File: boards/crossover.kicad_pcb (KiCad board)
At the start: 2 copper layers, 44 parts, among them CON1 12VDC Power, J1 JACK_TRS_6PINS, U1 TL074, U2 TL074

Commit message: upadated boards
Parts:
- removed CON1: 12VDC Power, Connect:BARREL_JACK
- added C23: 100n, Capacitors_ThroughHole:C_Disc_D6_P5, F.Cu at (227.3, 127.3)
- added C24: 100n, Capacitors_ThroughHole:C_Disc_D6_P5, F.Cu at (241.6, 108.7)
- added C25: 100n, Capacitors_ThroughHole:C_Disc_D6_P5, F.Cu at (250.2, 97.7)
- added C26: 100n, Capacitors_ThroughHole:C_Disc_D6_P5, F.Cu at (281.5, 69.3)
- added C27: 100n, Capacitors_ThroughHole:C_Disc_D6_P5, F.Cu at (233.1, 118.2)
- added C28: 100n, Capacitors_ThroughHole:C_Disc_D6_P5, F.Cu at (257.8, 97.4)
- added D1: Diode_Bridge, Diodes_ThroughHole:Diode_Bridge_15.7x15.7, F.Cu at (219.2, 69.4)
- added P1: 12-0-12, Terminal_Blocks:TerminalBlock_Pheonix_MKDS1.5-3pol, F.Cu at (187.8, 109.8)
- added R19: 2RH, Resistors_ThroughHole:Resistor_Horizontal_RM10mm, F.Cu at (231.7, 89.8)
- added U3: TDA7292, TO_SOT_Packages_THT:Multiwatt_15_Vertical, F.Cu at (169.5, 76.5)
- C1, C2: value 220u -> 100n; footprint Capacitors_ThroughHole:C_Radial_D10_L13_P5 -> Capacitors_ThroughHole:C_Disc_D3_P2.5
- C10, C17, C18: value 200n -> 100n; footprint Capacitors_SMD:C_0603_HandSoldering -> Capacitors_ThroughHole:C_Disc_D6_P5
- C11, C12, C19, C20, C21, C22, C5, C6, C7, C8, C9: footprint Capacitors_SMD:C_0603_HandSoldering -> Capacitors_ThroughHole:C_Disc_D6_P5
- C13, C14, C15, C16: footprint Capacitors_SMD:C_0603_HandSoldering -> Capacitors_ThroughHole:C_Disc_D3_P2.5
- C3: value 100n -> 6800u; footprint Capacitors_SMD:C_0603_HandSoldering -> Capacitors_ThroughHole:C_Radial_D16_L31.5_P7.5
- C4: value 200n -> 6800u; footprint Capacitors_SMD:C_0603_HandSoldering -> Capacitors_ThroughHole:C_Radial_D16_L31.5_P7.5
- R1: value 4K7 -> 100; footprint Resistors_ThroughHole:Resistor_Horizontal_RM15mm -> Resistors_ThroughHole:Resistor_Horizontal_RM10mm
- R10, R12, R14, R16, R18, R5, R9: footprint Resistors_ThroughHole:Resistor_Horizontal_RM15mm -> Resistors_ThroughHole:Resistor_Horizontal_RM10mm
- R11: value RL -> 2RH; footprint Resistors_ThroughHole:Resistor_Horizontal_RM15mm -> Resistors_ThroughHole:Resistor_Horizontal_RM10mm
- R13, R4, R8: value RH -> RL; footprint Resistors_ThroughHole:Resistor_Horizontal_RM15mm -> Resistors_ThroughHole:Resistor_Horizontal_RM10mm
- R15, R7: value RL -> RH; footprint Resistors_ThroughHole:Resistor_Horizontal_RM15mm -> Resistors_ThroughHole:Resistor_Horizontal_RM10mm
- R17: value 2RH -> RL; footprint Resistors_ThroughHole:Resistor_Horizontal_RM15mm -> Resistors_ThroughHole:Resistor_Horizontal_RM10mm
- R2: value 4K7 -> something bigg-ish; footprint Resistors_ThroughHole:Resistor_Horizontal_RM15mm -> Resistors_ThroughHole:Resistor_Horizontal_RM10mm
- R3: value RL -> something bigg-sh; footprint Resistors_ThroughHole:Resistor_Horizontal_RM15mm -> Resistors_ThroughHole:Resistor_Horizontal_RM10mm
- R6: value 2RH -> RH; footprint Resistors_ThroughHole:Resistor_Horizontal_RM15mm -> Resistors_ThroughHole:Resistor_Horizontal_RM10mm
- moved C8 139.7 mm to (265.3, 87.9)
- moved C7 120.3 mm to (241.6, 117.9)
- moved C6 115.7 mm to (257.7, 106.5)
- moved R4 112.1 mm to (234.7, 69.3)
- moved R5 92.3 mm to (218.5, 89.8)
- moved C2 83.1 mm to (180.2, 88.6)
- moved C5 79.9 mm to (250.2, 106.8)
- moved J1 78.3 mm to (201.2, 70.5)
- moved R9 73.8 mm to (247.9, 69.3)
- moved C16 64.5 mm to (234.7, 126.3)
- moved R10 62.6 mm to (199.5, 121.3)
- moved R2 59.2 mm to (170.3, 127.4)
- moved R11 56.0 mm to (228.7, 108.7)
- moved C1 55.9 mm to (180.2, 95.7)
- moved R3 55.9 mm to (204.4, 89.8)
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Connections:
- C1 pad 1: +6V -> +12V
- C11 pad 2: Net-(C11-Pad2) -> GND
- C13 pad 2: +6V -> +12V
- C14 pad 1: -6V -> -12V
- C15 pad 1: Net-(C15-Pad1) -> GND
- C15 pad 2: Net-(C15-Pad2) -> +12V
- C16 pad 1: Net-(C16-Pad1) -> -12V
- C16 pad 2: Net-(C16-Pad2) -> GND
- C18 pad 1: left_low_out -> Net-(C18-Pad1)
- C19 pad 1: Net-(C19-Pad1) -> right_low_out
- C19 pad 2: Net-(C15-Pad1) -> Net-(C19-Pad2)
- C2 pad 2: -6V -> -12V
- C20 pad 1: Net-(C20-Pad1) -> left_low_out
- C20 pad 2: Net-(C16-Pad1) -> Net-(C20-Pad2)
- C21 pad 2: GND -> Net-(C17-Pad1)
- C22 pad 2: GND -> Net-(C18-Pad1)
- C3 pad 1: Net-(C3-Pad1) -> +12V
- C3 pad 2: right_in -> GND
- C4 pad 1: Net-(C4-Pad1) -> GND
- C4 pad 2: Net-(C4-Pad2) -> -12V
- C5 pad 2: Net-(C3-Pad1) -> right_in
- C6 pad 1: Net-(C6-Pad1) -> Net-(C10-Pad2)
- C6 pad 2: GND -> left_in
- C7 pad 1: GND -> Net-(C25-Pad1)
- C7 pad 2: +6V -> Net-(C25-Pad2)
- C8 pad 1: -6V -> Net-(C8-Pad1)
- C8 pad 2: GND -> Net-(C8-Pad2)
- C9 pad 1: Net-(C11-Pad2) -> Net-(C9-Pad1)
- C9 pad 2: left_in -> Net-(C5-Pad1)
- J1 pad 4: Net-(J1-Pad4) -> (no net)
- J1 pad 5: Net-(J1-Pad5) -> (no net)
- J1 pad 6: Net-(J1-Pad6) -> (no net)
- R1 pad 1: +6V -> GND
- R1 pad 2: GND -> (no net)
- R10 pad 2: Net-(C11-Pad1) -> Net-(C9-Pad1)
- R11 pad 1: Net-(C4-Pad1) -> GND
- R11 pad 2: Net-(C17-Pad2) -> Net-(C10-Pad1)
- R12 pad 1: Net-(C10-Pad1) -> Net-(C25-Pad1)
- R12 pad 2: Net-(C18-Pad2) -> Net-(C19-Pad2)
- R13 pad 1: Net-(C15-Pad1) -> Net-(C8-Pad1)
- R13 pad 2: right_high_out -> Net-(C20-Pad2)
- R14 pad 1: Net-(C16-Pad1) -> Net-(C17-Pad1)
- R14 pad 2: left_high_out -> right_high_out
- R15 pad 1: Net-(C21-Pad1) -> Net-(C18-Pad1)
- R15 pad 2: Net-(C17-Pad2) -> left_high_out
- R16 pad 1: Net-(C22-Pad1) -> Net-(C23-Pad1)
- R16 pad 2: Net-(C18-Pad2) -> Net-(C19-Pad2)
- R17 pad 1: GND -> Net-(C24-Pad1)
- R17 pad 2: Net-(C19-Pad1) -> Net-(C20-Pad2)
- R18 pad 2: Net-(C20-Pad1) -> Net-(C21-Pad1)
- R2 pad 1: GND -> +12V
- R2 pad 2: -6V -> GND
- R3 pad 1: right_in -> GND
- R3 pad 2: Net-(C4-Pad2) -> -12V
- R4 pad 1: Net-(C3-Pad1) -> right_in
- R4 pad 2: Net-(C15-Pad2) -> Net-(C25-Pad2)
- R5 pad 1: Net-(C6-Pad1) -> left_in
- R5 pad 2: Net-(C4-Pad2) -> Net-(C8-Pad2)
- R6 pad 1: GND -> Net-(C5-Pad1)
- R6 pad 2: Net-(C5-Pad1) -> Net-(C17-Pad2)
- R7 pad 1: left_in -> Net-(C10-Pad2)
- R7 pad 2: Net-(C10-Pad2) -> Net-(C18-Pad2)
- R8 pad 1: Net-(C11-Pad2) -> Net-(C11-Pad1)
- R8 pad 2: Net-(C16-Pad2) -> Net-(C25-Pad2)
- R9 pad 2: Net-(C10-Pad2) -> Net-(C8-Pad2)
- U1 pad 1: Net-(C4-Pad1) -> Net-(C25-Pad1)
- U1 pad 10: Net-(C21-Pad1) -> Net-(C12-Pad1)
- U1 pad 11: -6V -> -12V
- U1 pad 12: Net-(C19-Pad1) -> Net-(C10-Pad1)
- U1 pad 13: right_high_out -> Net-(C18-Pad2)
- U1 pad 14: right_high_out -> Net-(C18-Pad2)
- U1 pad 2: Net-(C4-Pad1) -> Net-(C25-Pad1)
- U1 pad 3: Net-(C6-Pad1) -> Net-(C11-Pad1)
- U1 pad 4: +6V -> +12V
- U1 pad 5: Net-(C5-Pad1) -> Net-(C9-Pad1)
- U1 pad 6: Net-(C15-Pad2) -> Net-(C17-Pad2)
- U1 pad 7: Net-(C15-Pad2) -> Net-(C17-Pad2)
- U1 pad 8: Net-(C17-Pad1) -> Net-(C8-Pad1)
- U1 pad 9: Net-(C17-Pad1) -> Net-(C8-Pad1)
- U2 pad 1: Net-(C10-Pad1) -> right_high_out
- U2 pad 10: Net-(C20-Pad1) -> Net-(C23-Pad1)
- U2 pad 11: -6V -> (no net)
- U2 pad 12: Net-(C22-Pad1) -> Net-(C24-Pad1)
- U2 pad 2: Net-(C10-Pad1) -> right_high_out
- U2 pad 3: Net-(C12-Pad1) -> Net-(C21-Pad1)
- U2 pad 4: +6V -> (no net)
- U2 pad 5: Net-(C11-Pad1) -> Net-(C22-Pad1)
- U2 pad 6: Net-(C16-Pad2) -> left_high_out
- U2 pad 7: Net-(C16-Pad2) -> left_high_out
- U2 pad 8: left_high_out -> right_low_out
- U2 pad 9: left_high_out -> right_low_out
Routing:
- net Net-(C10-Pad2): track 155.9 -> 0.00 mm, vias 2 -> 0
- net Net-(C12-Pad1): track 153.7 -> 0.00 mm, vias 1 -> 0
- net Net-(C21-Pad1): track 142.9 -> 0.00 mm, vias 1 -> 0
- net GND: track 141.8 -> 0.00 mm
- net Net-(C10-Pad1): track 121.5 -> 0.00 mm
- net +6V: track 113.5 -> 0.00 mm, vias 1 -> 0
- net Net-(C11-Pad1): track 90.0 -> 0.00 mm, vias 1 -> 0
- net right_high_out: track 84.7 -> 0.00 mm, vias 1 -> 0
- net Net-(C17-Pad2): track 75.8 -> 0.00 mm, vias 1 -> 0
- net -6V: track 72.8 -> 0.00 mm
- net Net-(C22-Pad1): track 70.5 -> 0.00 mm
- net Net-(C20-Pad1): track 69.1 -> 0.00 mm, vias 1 -> 0
- net left_in: track 64.3 -> 0.00 mm, vias 1 -> 0
- net Net-(C4-Pad2): track 42.8 -> 0.00 mm
- net left_high_out: track 42.5 -> 0.00 mm
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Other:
- net class Default: via_dia 0.381 -> 0.6858; via_drill 0.254 -> 0.3302
- net class Power: via_dia 0.381 -> 0.6858; via_drill 0.254 -> 0.3302
- rule via_min_drill: 0.254 -> 0.3302
- rule via_min_size: 0.381 -> 0.6858

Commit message: some board work, added windows appveyor file
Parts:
- added REF***: OSHW-Logo_5.7x6mm_SilkScreen, Symbols:OSHW-Logo_5.7x6mm_SilkScreen, F.Cu at (132.1, 61.0)
- added REF***: KiCad-Logo2_6mm_SilkScreen, Symbols:KiCad-Logo2_6mm_SilkScreen, F.Cu at (119.4, 61.0)
- added U5: LM7815CT, TO-220, F.Cu at (215.9, 66.0)
- added U6: LM7915CT, TO-220, F.Cu at (212.1, 74.9)
- R2: value something bigg-ish -> 1K 1W
- R3: value something bigg-sh -> 1K 1W
- moved C26 135.1 mm to (147.3, 85.0), turned to 90 degrees
- moved C8 107.0 mm to (158.8, 97.8)
- moved C13 104.6 mm to (198.1, 138.4)
- moved C14 95.4 mm to (172.7, 119.4)
- moved R9 95.0 mm to (154.9, 88.9)
- moved C16 75.0 mm to (160.0, 119.4)
- moved C12 71.7 mm to (172.7, 83.8)
- moved R10 68.8 mm to (132.1, 108.0)
- moved C11 67.9 mm to (207.0, 108.0)
- moved J1 66.4 mm to (236.2, 127.0)
- moved R4 66.4 mm to (217.2, 133.3)
- moved C15 65.8 mm to (198.1, 144.8)
- moved C6 62.9 mm to (212.1, 149.9)
- moved D1 62.5 mm to (181.6, 119.4)
- moved U2 61.6 mm to (231.1, 92.7)
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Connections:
- C26 pad 1: (no net) -> Net-(C26-Pad1)
- C26 pad 2: (no net) -> Net-(C26-Pad2)
- C27 pad 1: (no net) -> right_low_out
- C27 pad 2: (no net) -> Net-(C19-Pad2)
- C28 pad 1: (no net) -> left_low_out
- C28 pad 2: (no net) -> Net-(C20-Pad2)
- C8 pad 1: Net-(C8-Pad1) -> Net-(C26-Pad1)
- C8 pad 2: Net-(C8-Pad2) -> Net-(C26-Pad2)
- J1 pad 2: right_in -> left_in
- J1 pad 3: left_in -> right_in
- R13 pad 1: Net-(C8-Pad1) -> Net-(C26-Pad1)
- R5 pad 2: Net-(C8-Pad2) -> Net-(C26-Pad2)
- R9 pad 2: Net-(C8-Pad2) -> Net-(C26-Pad2)
- U1 pad 8: Net-(C8-Pad1) -> Net-(C26-Pad1)
- U1 pad 9: Net-(C8-Pad1) -> Net-(C26-Pad1)
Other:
- board outline added: 160 x 105.4 mm
- net class Audio Out added: clearance 0.254, trace_width 1.27, via_dia 0.6858, via_drill 0.3302

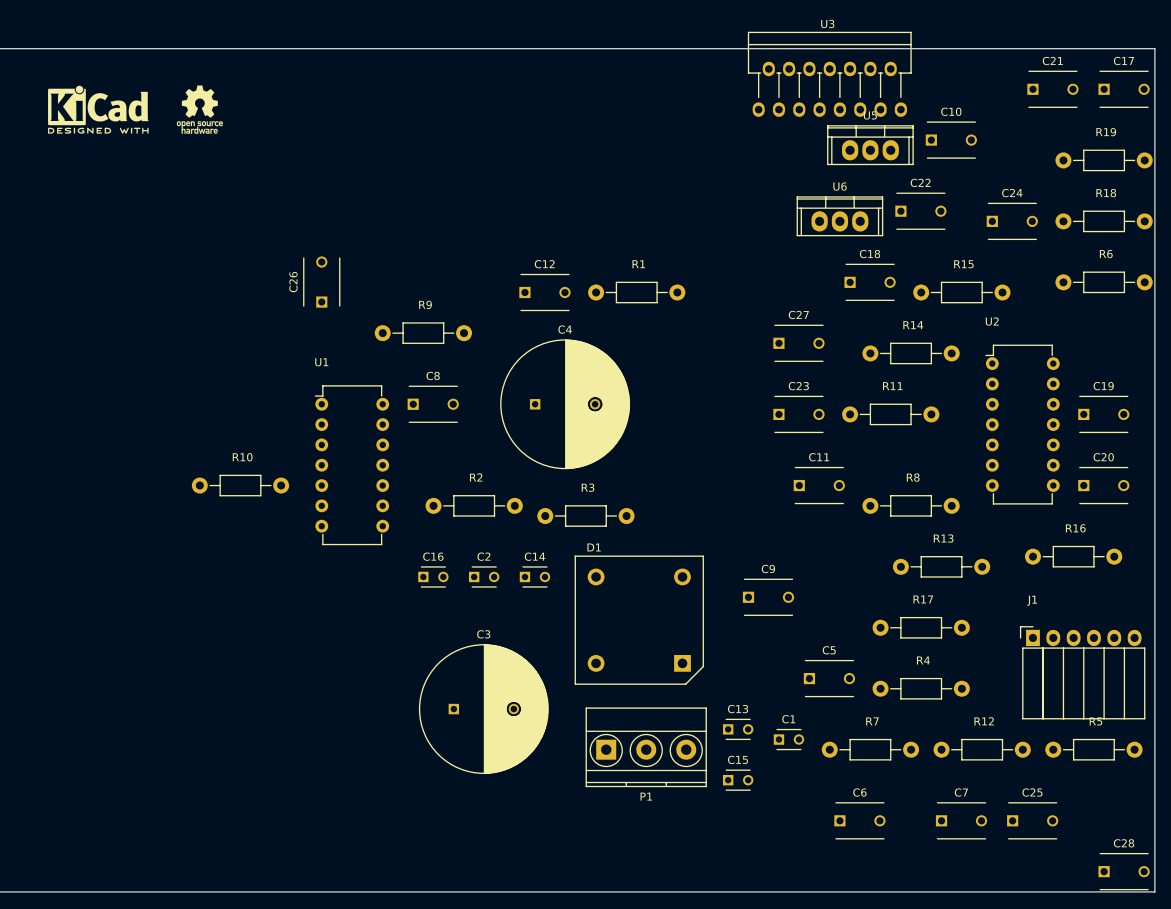
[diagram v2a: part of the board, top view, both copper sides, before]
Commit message: lots of updates, only trigger appveyor builds explicitly in commit message
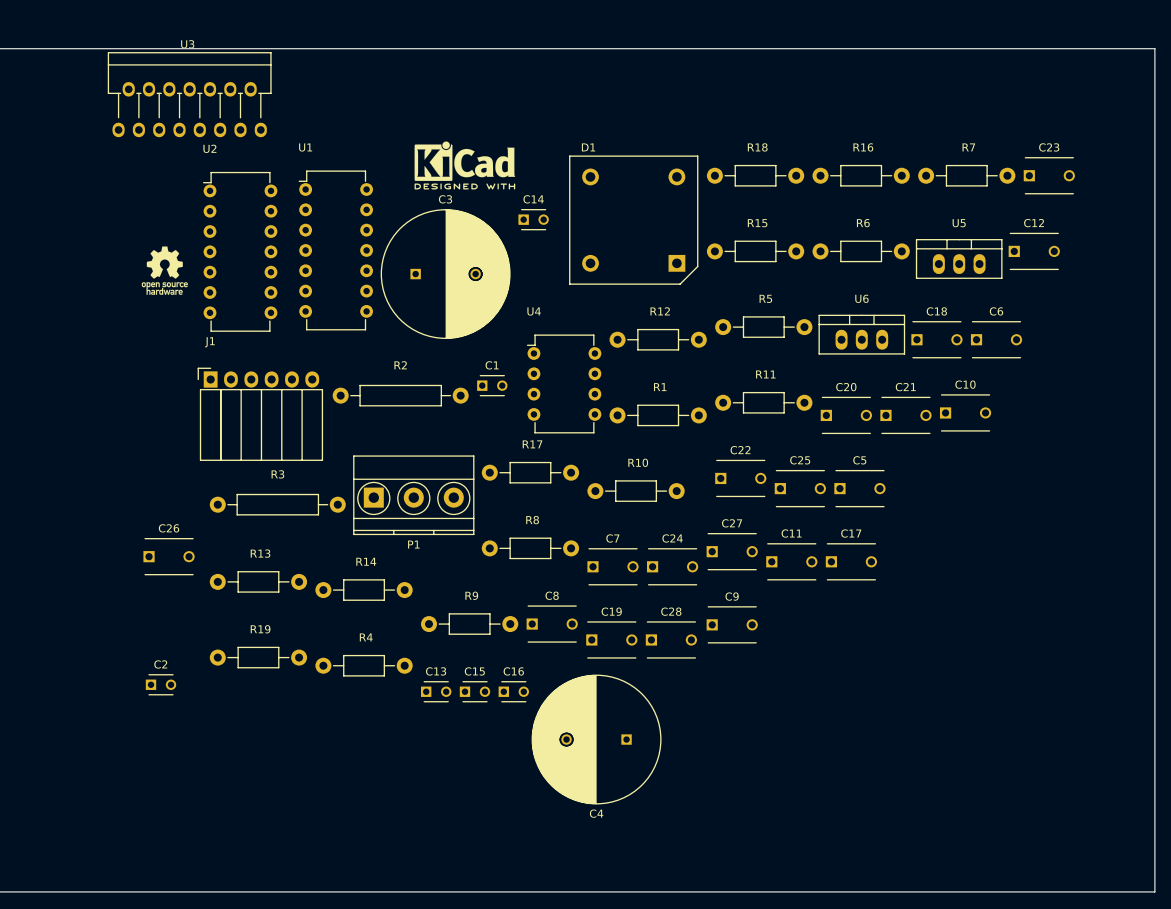
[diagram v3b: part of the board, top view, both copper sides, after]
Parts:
- added U4: TL072, Housings_DIP:DIP-8_W7.62mm, F.Cu at (173.8, 91.4)
- R2, R3: footprint Resistors_ThroughHole:Resistor_Horizontal_RM10mm -> Resistors_ThroughHole:Resistor_Horizontal_RM15mm
- U5, U6: footprint TO-220 -> TO_SOT_Packages_THT:TO-220_Neutral123_Vertical
- moved R19 122.6 mm to (134.3, 129.5)
- moved J1 107.7 mm to (133.4, 94.7)
- moved U2 100.1 mm to (133.3, 71.1)
- moved R13 85.4 mm to (134.3, 120.0)
- moved U3 80.1 mm to (121.9, 63.5)
- moved R14 74.5 mm to (147.5, 121.0)
- moved R7 72.7 mm to (222.9, 69.2)
- moved R4 69.7 mm to (147.5, 130.5)
- moved C17 68.2 mm to (211.0, 117.5)
- moved C19 67.7 mm to (181.1, 127.3)
- moved R5 67.0 mm to (197.5, 88.1)
- moved R12 65.3 mm to (184.3, 89.7)
- moved C28 63.6 mm to (188.5, 127.3)
- moved C6 62.5 mm to (229.2, 89.7)
- moved C12 61.4 mm to (233.9, 78.7)
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
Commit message: updates
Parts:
- removed REF***: OSHW-Logo_5.7x6mm_SilkScreen, Symbols:OSHW-Logo_5.7x6mm_SilkScreen
- removed REF***: KiCad-Logo2_6mm_SilkScreen, Symbols:KiCad-Logo2_6mm_SilkScreen
- removed U5: LM7815CT, TO_SOT_Packages_THT:TO-220_Neutral123_Vertical
- removed U6: LM7915CT, TO_SOT_Packages_THT:TO-220_Neutral123_Vertical
- added C29: 100n, Capacitors_ThroughHole:C_Disc_D6_P5, F.Cu at (121.9, 93.1)
- added C30: 100n, Capacitors_ThroughHole:C_Disc_D6_P5, F.Cu at (181.4, 120.8)
- added R20: RH, Resistors_ThroughHole:Resistor_Horizontal_RM10mm, F.Cu at (197.0, 76.1)
- added R21: RH, Resistors_ThroughHole:Resistor_Horizontal_RM10mm, F.Cu at (182.5, 87.2)
- added R22: RH, Resistors_ThroughHole:Resistor_Horizontal_RM10mm, F.Cu at (197.0, 66.7)
- added R23: RH, Resistors_ThroughHole:Resistor_Horizontal_RM10mm, F.Cu at (150.0, 113.5)
- added RV1: DUAL_POT, Pin_Headers:Pin_Header_Straight_2x03, F.Cu at (124.6, 81.4)
- C13, C15, C16: footprint Capacitors_ThroughHole:C_Disc_D3_P2.5 -> Capacitors_ThroughHole:C_Disc_D6_P5
- C2: value 100n -> 6800u; footprint Capacitors_ThroughHole:C_Disc_D3_P2.5 -> Capacitors_ThroughHole:C_Radial_D16_L31.5_P7.5
- C21, C26, C6, C9: footprint Capacitors_ThroughHole:C_Disc_D6_P5 -> Capacitors_ThroughHole:C_Disc_D3_P2.5
- C3, C4: value 6800u -> 100n; footprint Capacitors_ThroughHole:C_Radial_D16_L31.5_P7.5 -> Capacitors_ThroughHole:C_Disc_D3_P2.5
- C5: value 100n -> 6800u; footprint Capacitors_ThroughHole:C_Disc_D6_P5 -> Capacitors_ThroughHole:C_Radial_D16_L31.5_P7.5
- R10, R11, R18, R19: value 2RH -> RH
- R14, R15, R6, R7: value RH -> RL
- R16, R17, R8, R9: value RL -> RH
- U1: value TL074 -> TL072; footprint Housings_DIP:DIP-14_W7.62mm -> Housings_DIP:DIP-8_W7.62mm
- U4: value TL072 -> TL074; footprint Housings_DIP:DIP-8_W7.62mm -> Housings_DIP:DIP-14_W7.62mm
- moved C6 99.7 mm to (138.6, 131.4)
- moved R19 98.5 mm to (210.2, 66.7)
- moved R14 93.3 mm to (223.4, 66.7)
- moved C9 80.6 mm to (130.3, 78.8)
- moved R1 79.9 mm to (110.8, 130.6)
- moved C12 77.8 mm to (175.6, 130.2)
- moved C5 77.7 mm to (135.2, 96.7)
- moved C16 72.1 mm to (223.5, 85.3)
- moved C27 66.6 mm to (131.2, 131.0)
- moved C2 66.0 mm to (152.7, 72.5)
- moved C15 65.1 mm to (217.4, 94.8)
- moved C28 64.9 mm to (123.7, 131.0)
- moved R6 64.8 mm to (150.0, 104.1)
- moved U4 62.9 mm to (111.8, 81.5)
- moved C14 58.6 mm to (158.0, 131.4)
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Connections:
- C10 pad 1: Net-(C10-Pad1) -> right_low_out
- C11 pad 1: Net-(C11-Pad1) -> right_low_out
- C11 pad 2: GND -> Net-(C10-Pad2)
- C13 pad 1: GND -> Net-(C13-Pad1)
- C13 pad 2: +12V -> GND
- C15 pad 1: GND -> Net-(C15-Pad1)
- C15 pad 2: +12V -> right_in
- C16 pad 1: -12V -> Net-(C16-Pad1)
- C16 pad 2: GND -> Net-(C15-Pad1)
- C18 pad 2: Net-(C18-Pad2) -> Net-(C17-Pad1)
- C19 pad 1: right_low_out -> Net-(C19-Pad1)
- C2 pad 1: GND -> +12V
- C2 pad 2: -12V -> GND
- C20 pad 1: left_low_out -> Net-(C19-Pad1)
- C20 pad 2: Net-(C20-Pad2) -> Net-(C19-Pad2)
- C21 pad 1: Net-(C21-Pad1) -> GND
- C21 pad 2: Net-(C17-Pad1) -> +12V
- C22 pad 1: Net-(C22-Pad1) -> left_low_out
- C22 pad 2: Net-(C18-Pad1) -> Net-(C22-Pad2)
- C23 pad 1: Net-(C23-Pad1) -> left_low_out
- C23 pad 2: GND -> Net-(C22-Pad2)
- C25 pad 2: Net-(C25-Pad2) -> GND
- C26 pad 1: Net-(C26-Pad1) -> -12V
- C26 pad 2: Net-(C26-Pad2) -> GND
- C27 pad 1: right_low_out -> Net-(C27-Pad1)
- C27 pad 2: Net-(C19-Pad2) -> left_in
- C28 pad 1: left_low_out -> Net-(C28-Pad1)
- C28 pad 2: Net-(C20-Pad2) -> Net-(C27-Pad1)
- C3 pad 1: +12V -> GND
- C3 pad 2: GND -> +12V
- C5 pad 1: Net-(C5-Pad1) -> GND
- C5 pad 2: right_in -> -12V
- C6 pad 1: Net-(C10-Pad2) -> -12V
- C6 pad 2: left_in -> GND
- C7 pad 1: Net-(C25-Pad1) -> Net-(C7-Pad1)
- C7 pad 2: Net-(C25-Pad2) -> Net-(C7-Pad2)
- C8 pad 1: Net-(C26-Pad1) -> Net-(C7-Pad1)
- C8 pad 2: Net-(C26-Pad2) -> Net-(C7-Pad2)
- C9 pad 1: Net-(C9-Pad1) -> GND
- C9 pad 2: Net-(C5-Pad1) -> +12V
- J1 pad 2: left_in -> Net-(J1-Pad2)
- J1 pad 3: right_in -> Net-(J1-Pad3)
- R10 pad 1: GND -> Net-(R10-Pad1)
- R10 pad 2: Net-(C9-Pad1) -> Net-(C16-Pad1)
- R11 pad 1: GND -> Net-(R11-Pad1)
- R11 pad 2: Net-(C10-Pad1) -> Net-(C18-Pad1)
- R12 pad 1: Net-(C25-Pad1) -> left_in
- R13 pad 1: Net-(C26-Pad1) -> Net-(C24-Pad1)
- R13 pad 2: Net-(C20-Pad2) -> Net-(C19-Pad2)
- R14 pad 1: Net-(C17-Pad1) -> Net-(C19-Pad1)
- R14 pad 2: right_high_out -> Net-(C22-Pad2)
- R15 pad 1: Net-(C18-Pad1) -> Net-(C25-Pad1)
- R15 pad 2: left_high_out -> Net-(C22-Pad2)
- R16 pad 1: Net-(C23-Pad1) -> Net-(C27-Pad1)
- R16 pad 2: Net-(C19-Pad2) -> Net-(C29-Pad2)
- R17 pad 1: Net-(C24-Pad1) -> Net-(C29-Pad1)
- R17 pad 2: Net-(C20-Pad2) -> left_high_out
- R18 pad 1: GND -> Net-(R18-Pad1)
- R18 pad 2: Net-(C21-Pad1) -> Net-(C28-Pad1)
- R19 pad 1: GND -> Net-(R19-Pad1)
- R19 pad 2: Net-(C22-Pad1) -> Net-(C30-Pad1)
- R4 pad 2: Net-(C25-Pad2) -> Net-(C7-Pad2)
- R5 pad 1: left_in -> Net-(C12-Pad1)
- R5 pad 2: Net-(C26-Pad2) -> Net-(C7-Pad2)
- R6 pad 1: Net-(C5-Pad1) -> Net-(C7-Pad1)
- R6 pad 2: Net-(C17-Pad2) -> Net-(C10-Pad2)
- R7 pad 1: Net-(C10-Pad2) -> Net-(C13-Pad1)
- R7 pad 2: Net-(C18-Pad2) -> Net-(C10-Pad2)
- R8 pad 1: Net-(C11-Pad1) -> Net-(C15-Pad1)
- R8 pad 2: Net-(C25-Pad2) -> Net-(C17-Pad2)
- R9 pad 1: Net-(C12-Pad1) -> Net-(C17-Pad1)
- R9 pad 2: Net-(C26-Pad2) -> right_high_out
- U1 pad 1: Net-(C25-Pad1) -> left_in
- U1 pad 2: Net-(C25-Pad1) -> left_in
- U1 pad 3: Net-(C11-Pad1) -> Net-(RV1-Pad2)
- U1 pad 4: +12V -> -12V
- U1 pad 5: Net-(C9-Pad1) -> Net-(RV1-Pad5)
- U1 pad 6: Net-(C17-Pad2) -> right_in
- U1 pad 7: Net-(C17-Pad2) -> right_in
- U1 pad 8: Net-(C26-Pad1) -> +12V
- U2 pad 1: right_high_out -> Net-(C7-Pad1)
- U2 pad 10: Net-(C23-Pad1) -> Net-(C16-Pad1)
- U2 pad 11: (no net) -> -12V
- U2 pad 12: Net-(C24-Pad1) -> Net-(C18-Pad1)
- U2 pad 13: left_low_out -> right_high_out
- U2 pad 14: left_low_out -> right_high_out
- U2 pad 2: right_high_out -> Net-(C7-Pad1)
- U2 pad 3: Net-(C21-Pad1) -> Net-(C12-Pad1)
- U2 pad 4: (no net) -> +12V
- U2 pad 5: Net-(C22-Pad1) -> Net-(C13-Pad1)
- U2 pad 6: left_high_out -> right_low_out
- U2 pad 7: left_high_out -> right_low_out
- U2 pad 8: right_low_out -> Net-(C17-Pad2)
- U2 pad 9: right_low_out -> Net-(C17-Pad2)
- U4 pad 1: (no net) -> Net-(C19-Pad1)
- U4 pad 2: (no net) -> Net-(C19-Pad1)
- U4 pad 3: (no net) -> Net-(C24-Pad1)
- U4 pad 4: (no net) -> +12V
- U4 pad 5: (no net) -> Net-(C25-Pad1)
- U4 pad 6: (no net) -> left_low_out
- U4 pad 7: (no net) -> left_low_out
- U4 pad 8: (no net) -> Net-(C29-Pad2)
